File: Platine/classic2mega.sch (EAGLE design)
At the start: 25 parts, among them IC1 MEGA16-A, IC2 74HC157D, Q2 16MHz, U1 MCP1700_SOT23

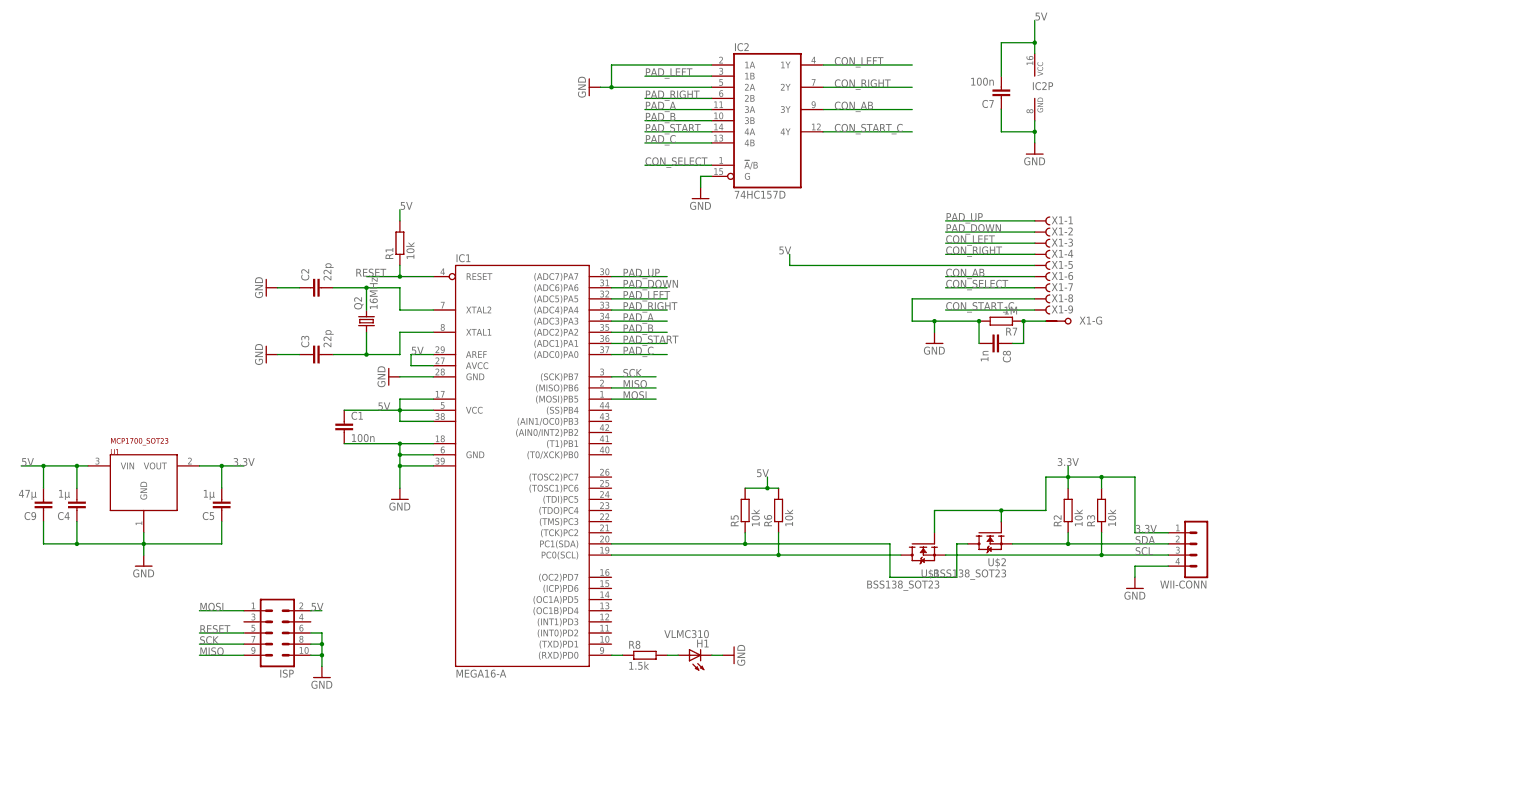
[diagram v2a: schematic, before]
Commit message: Change ICs to DIP packages
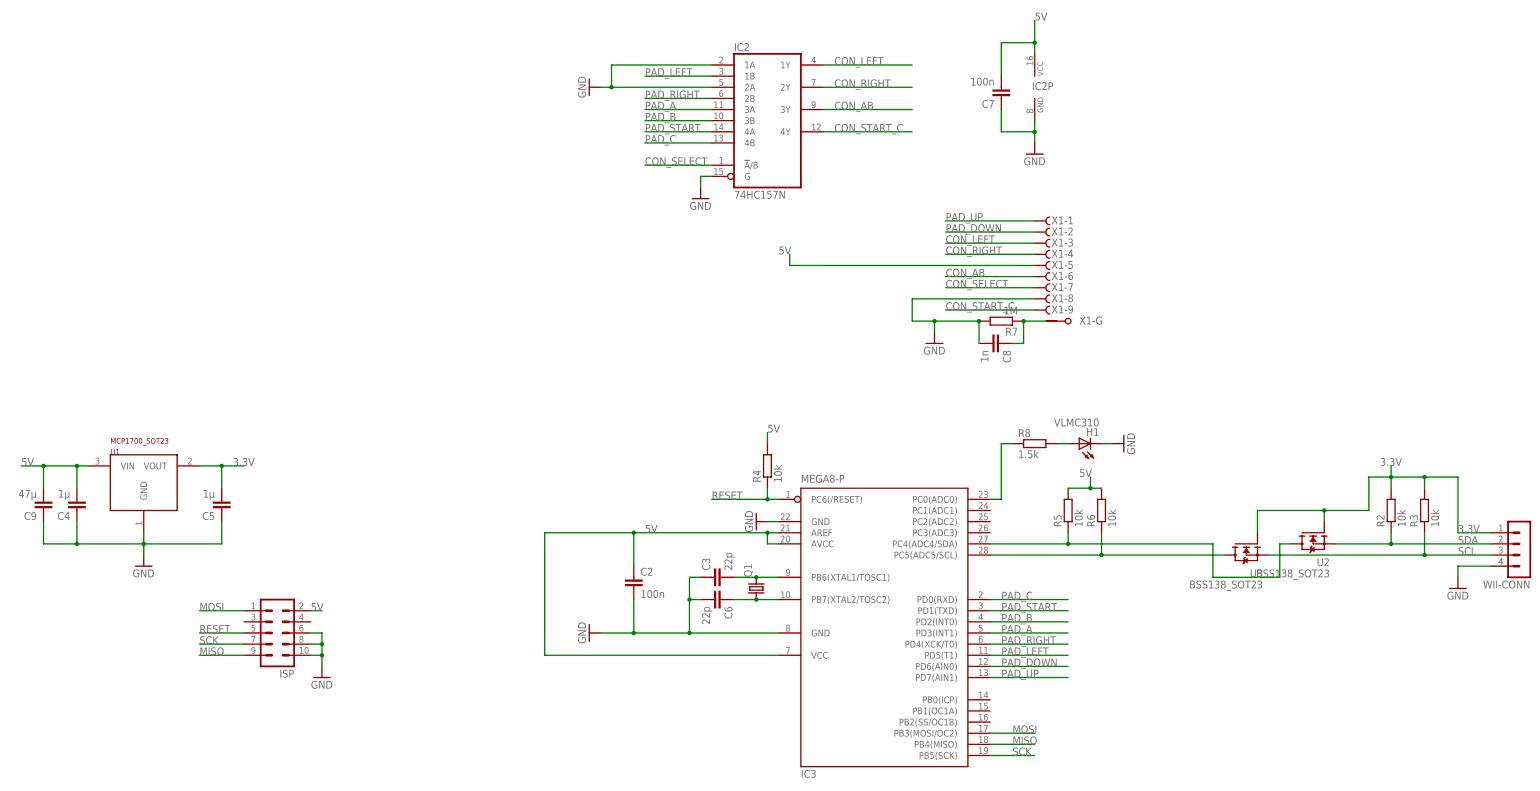
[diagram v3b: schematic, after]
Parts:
- removed C1: 100n, resistor:C-EUC0805K
- removed IC1: MEGA16-A, atmega16:MEGA16-A
- removed Q2: 16MHz, crystal:CRYSTALHC49S
- removed R1: 10k, resistor:R-EU_M0805
- removed U$1, U$2: BSS138_SOT23, BSS138:BSS138_SOT23
- added C6: 22p, resistor:C-EUC0805K
- added IC3: MEGA8-P, atmel:MEGA8-P
- added Q1: (no value), crystal:CRYSTALHC49S
- added R4: 10k, resistor:R-EU_M0805
- added U2, U3: BSS138_SOT23, BSS138:BSS138_SOT23
- C2: value 22p -> 100n
- IC2: value 74HC157D -> 74HC157N; device 74xx-eu:74HC157D -> 74xx-eu:74HC157N
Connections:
- removed net N$8: IC1.(RXD)PD0, R8.1
- new net N$5: C6.1, IC3.PB7(XTAL2/TOSC2), Q1.1
- net 3.3V: now also U2.G, U3.G; no longer U$1.G, U$2.G
- net 5V: now also C2.1, IC3.AREF, IC3.AVCC, IC3.VCC@1, R4.2; no longer C1.1, IC1.AREF, IC1.AVCC, IC1.VCC, IC1.VCC1, IC1.VCC2, R1.2
- net GND: now also C2.2, C6.2, IC3.GND, IC3.GND@1; no longer C1.2, C2.1, IC1.GND, IC1.GND1, IC1.GND2, IC1.GND@1
- net MISO: now also IC3.PB4(MISO); no longer IC1.(MISO)PB6
- net MOSI: now also IC3.PB3(MOSI/OC2); no longer IC1.(MOSI)PB5
- net N$1: now also IC3.PC4(ADC4/SDA), U2.D; no longer IC1.PC1(SDA), U$2.D
- net N$2: now also IC3.PC0(ADC0), R8.1; no longer C2.2, IC1.XTAL2, Q2.2
- net N$3: now also IC3.PB6(XTAL1/TOSC1), Q1.2; no longer IC1.XTAL1, Q2.1
- net N$4: now also IC3.PC5(ADC5/SCL), U3.D; no longer IC1.PC0(SCL), U$1.D
- net PAD_A: now also IC3.PD3(INT1); no longer IC1.(ADC3)PA3
- net PAD_B: now also IC3.PD2(INT0); no longer IC1.(ADC2)PA2
- net PAD_C: now also IC3.PD0(RXD); no longer IC1.(ADC0)PA0
- net PAD_DOWN: now also IC3.PD6(AIN0); no longer IC1.(ADC6)PA6
- net PAD_LEFT: now also IC3.PD5(T1); no longer IC1.(ADC5)PA5
- net PAD_RIGHT: now also IC3.PD4(XCK/T0); no longer IC1.(ADC4)PA4
- net PAD_START: now also IC3.PD1(TXD); no longer IC1.(ADC1)PA1
- net PAD_UP: now also IC3.PD7(AIN1); no longer IC1.(ADC7)PA7
- net RESET: now also IC3.PC6(/RESET), R4.1; no longer IC1.RESET, R1.1
- net SCK: now also IC3.PB5(SCK); no longer IC1.(SCK)PB7
- net SCL: now also U3.S; no longer U$1.S
- net SDA: now also U2.S; no longer U$2.S
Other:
- moved on the sheet: C2, C3, H1, R2, R3, R5, R6, R8, WII-CONN

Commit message: Change C9 to 1210 footprint
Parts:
- C9: device resistor:C-EUC0805K -> resistor:C-EUC1210
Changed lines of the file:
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@@
 <part name="R8" library="resistor" deviceset="R-EU_" device="M0805" value="1.5k"/>
 <part name="GND14" library="supply1" deviceset="GND" device=""/>
-<part name="C9" library="resistor" deviceset="C-EU" device="C0805K" value="47µ"/>
+<part name="C9" library="resistor" library_urn="urn:adsk.eagle:library:348" deviceset="C-EU" device="C1210" package3d_urn="urn:adsk.eagle:package:26139/1" value="47µ"/>
 <part name="H1" library="VLMC310" deviceset="VLMC310" device=""/>
 <part name="U3" library="BSS138" deviceset="BSS138_SOT23" device=""/>
